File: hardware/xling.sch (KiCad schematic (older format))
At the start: 51 parts, among them J3 MCP73831, J4 USB_OTG, J5 AVR ISP, J6 Battery, Q1 TP0610T, SW2 Up, SW3 Select, SW4 Down, U1 LT1109CZ-12, U2 ATMEGA328P-AU, U3 DEP_128064I, U4 MCP1640B-CH, U5 LM1117-3.3, Y1 8MHz

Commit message: patch 0.1.18: Add new KiCad modules and scheme changes.
Signed-off-by: Dmitry Salychev <darkness.bsd@gmail.com>
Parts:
- removed C12: 2.2uF, Capacitors_SMD:C_0603, symbol C
- removed D1: charging, LEDs:LED_0603, symbol LED
- removed D2: charged, LEDs:LED_0805, symbol LED
- added C9: 1pF, Capacitors_SMD:C_0805, symbol C
- added Q2: NTR0202PL, TO_SOT_Packages_SMD:SOT-23, symbol NTR2101P
- added Q3: NTA4153N, Xling Footprints:SC-75_SOT-416, symbol 2N7000
- added R10: 100K, Resistors_SMD:R_1206, symbol R
- J6: footprint Pin_Headers:Pin_Header_Straight_1x02 -> Xling Footprints:Pin_Header_Straight_1x02
- R1, R5: value 470R -> 100K; Model CRCW1206470RFKTABC -> (none)
- U5: footprint TO_SOT_Packages_SMD:SOT-223-3Lead_TabPin2 -> Xling Footprints:SOT-223-3Lead_TabPin2
- Y1: footprint Crystals:Crystal_HC49-SD_SMD -> Xling Footprints:Crystal_HC49-SD_SMD
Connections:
- net +12V: now also R5.1, Q2.2 (S); no longer U3.23 (VCC)
- net +3V3: now also R1.1; no longer U3.9 (RES#)
- net GND: now also C9.2, Q3.1 (S), R10.2; no longer R5.1
- net BAT_STAT: now reaches J3.1 (STAT)
- net BAT_STAT: now also U2.9 ((PCINT21/OC0B/T1)PD5)
- net at R5.2: now also Q2.1 (G), Q3.3 (D)
- net at C4.1, D5.1 (K), Q1.1 (G)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: no longer R1.1
- net OLED_RES: now reaches R1.2
- net OLED_RES: now also U2.1 ((PCINT19/OC2B/INT1)PD3), U3.9 (RES#)
- net OLED_PWR: now reaches U2.2 ((PCINT20/XCK/T0)PD4)
- net OLED_PWR: now also Q3.2 (G), R10.1
- new net OLED_VCC: C9.1, Q2.3 (D), U3.23 (VCC)
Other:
- note added: "*\n* Including model files\n*\n*.include NTA4001NT1.LIB\n.include NTA4153N.REV0.LIB\n.include NTR0202PL.REV0.LIB\n*\n* Components of the scheme\n*\nR1 0 1 100k\nR2 2 3 100k\n* R3 - pull-down resistor to prove an output is floating contact when\n* XQ2 is closed\n*R3 4 0 100k\nC1 4 0 1p\nXQ1 2 1 0 nta4153n\nXQ2 4 2 3 ntr0202plt1\nVIN 1 0 pulse (0 3.15 2ms 0ns 0ms 5ms 10ms)\nVDD 3 0 pwl (0 0 0ms 0 0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"
- note added: "12V OLED Vcc switch"
- note added: "12V OLED Vcc switch (transient analysis)"
- note added: "3.3V power supply and battery charger"
- note added: "Buttons for microcontroller"
- note added: "Controller:\nVDD:\nVCC:\nMode:\nAddress:"
- note added: "It is recommended to set Iref to 10±2uA:\nR2 = (Vcc-3)/Iref = (12V-3V)/10uA = 900kΩ"
- note added: "Microcontroller ATMEGA328P"
- note added: "OLED display 128x64"
- note added: "SSD1309ZC\n2.8-3.3V\n12V\nI2C\n0x3D"
- note added: "The main idea of the scheme is to produce 3.3V. This can\nbe done by providing a 5V USB connection to power the whole\nscheme via LM1117 and charge a 3.7V Li-Ion or Li-Polymer\nbattery using MCP73831 on the one hand. On the other hand\n- the whole scheme can work autonomously using the battery\nand change its voltage down to 3.3V via MCP1640B."
- note added: "This switch is based on N-Channel and\nP-Channel MOSFETs to power on and off\nOLED display. This is necessary to use\na logic level 3.3V to switch 12V and\nleave Vcc contact floating when\nNTR0202PL is closed."
- note removed: "3.7V Li-Ion, Li-Polymer Battery Charger Curcuit with Load Sharing"
- note removed: "Controller:\nVDD:\nMode:\nAddress:"
- note removed: "It is recommended to set Iref to 10±2uA:\nR = (Vcc-3)/Iref = (12V-3V)/10uA = 900kΩ"
- note removed: "SSD1309ZC\n2.8-3.3V\nI2C\n0x3D"
- note removed: "both are tantalum capacitors\nAVX TAJB106K006RNJ\n"
- moved on the sheet: C1, C10, C11, C13, C15, C18, C19, C2, C20, C3, C4, C5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

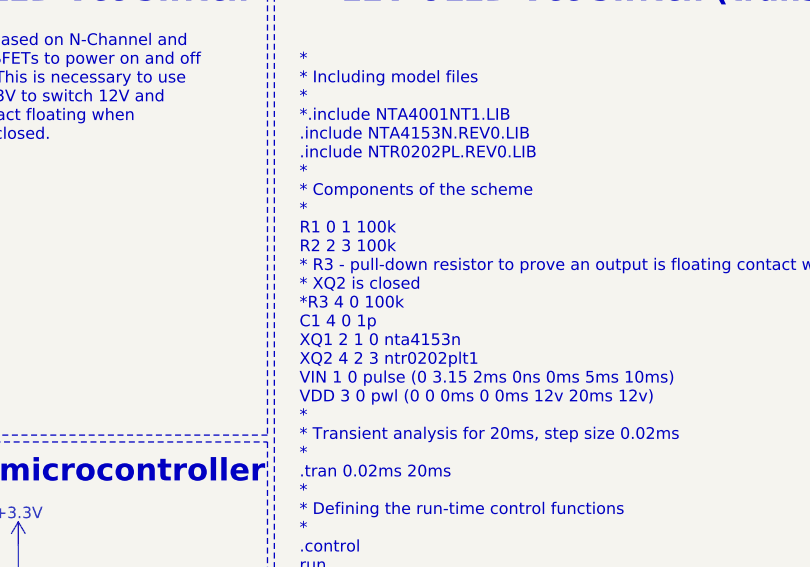
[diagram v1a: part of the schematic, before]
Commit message: patch 0.1.20: Update PCB and prepare gerber files for production.
Signed-off-by: Dmitry Salychev <darkness.bsd@gmail.com>
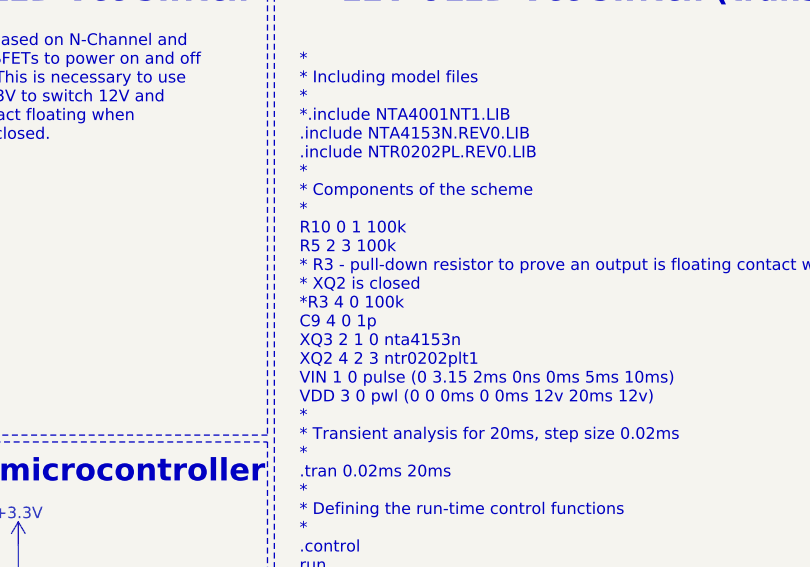
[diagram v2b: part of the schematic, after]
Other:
- note added: "*\n* Including model files\n*\n*.include NTA4001NT1.LIB\n.include NTA4153N.REV0.LIB\n.include NTR0202PL.REV0.LIB\n*\n* Components of the scheme\n*\nR10 0 1 100k\nR5 2 3 100k\n* R3 - pull-down resistor to prove an output is floating contact when\n* XQ2 is closed\n*R3 4 0 100k\nC9 4 0 1p\nXQ3 2 1 0 nta4153n\nXQ2 4 2 3 ntr0202plt1\nVIN 1 0 pulse (0 3.15 2ms 0ns 0ms 5ms 10ms)\nVDD 3 0 pwl (0 0 0ms 0 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"
- note removed: "*\n* Including model files\n*\n*.include NTA4001NT1.LIB\n.include NTA4153N.REV0.LIB\n.include NTR0202PL.REV0.LIB\n*\n* Components of the scheme\n*\nR1 0 1 100k\nR2 2 3 100k\n* R3 - pull-down resistor to prove an output is floating contact when\n* XQ2 is closed\n*R3 4 0 100k\nC1 4 0 1p\nXQ1 2 1 0 nta4153n\nXQ2 4 2 3 ntr0202plt1\nVIN 1 0 pulse (0 3.15 2ms 0ns 0ms 5ms 10ms)\nVDD 3 0 pwl (0 0 0ms 0 0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"
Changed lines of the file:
@@
 Title "Xling Schematic"
 Date ""
-Rev "0.1.18"
-Comp "Terrible Terminal Inc."
+Rev "0.1.20"
+Comp ""
 Comment1 ""
 Comment2 ""
@@
 This switch is based on N-Channel and\nP-Channel MOSFETs to power on and off\nOLED display. This is necessary to use\na logic level 3.3V to switch 12V and\nleave Vcc contact floating when\nNTR0202PL is closed.
 Text Notes 12340 3970 0    51   ~ 0
-*\n* Including model files\n*\n*.include NTA4001NT1.LIB\n.include NTA4153N.REV0.LIB\n.include NTR0202PL.REV0.LIB\n*\n* Components of the scheme\n*\nR1 0 1 100k\nR2 2 3 100k\n* R3 - pull-down resistor to prove an output is floating contact when\n* XQ2 is closed\n*R3 4 0 100k\nC1 4 0 1p\nXQ1 2 1 0 nta4153n\nXQ2 4 2 3 ntr0202plt1\nVIN 1 0 pulse (0 3.15 2ms 0ns 0ms 5ms 10ms)\nVDD 3 0 pwl (0 0 0ms 0 0ms 12v 20ms 12v)\n*\n* Transient analysis for 20ms, step size 0.02ms\n*\n.tran 0.02ms 20ms\n*\n* Defining the run-time control functions\n*\n.control\nrun\n*\n* Plotting input and output voltages\n*\nplot v(1) v(4)\n.endc\n.end
+*\n* Including model files\n*\n*.include NTA4001NT1.LIB\n.include NTA4153N.REV0.LIB\n.include NTR0202PL.REV0.LIB\n*\n* Components of the scheme\n*\nR10 0 1 100k\nR5 2 3 100k\n* R3 - pull-down resistor to prove an output is floating contact when\n* XQ2 is closed\n*R3 4 0 100k\nC9 4 0 1p\nXQ3 2 1 0 nta4153n\nXQ2 4 2 3 ntr0202plt1\nVIN 1 0 pulse (0 3.15 2ms 0ns 0ms 5ms 10ms)\nVDD 3 0 pwl (0 0 0ms 0 0ms 12v 20ms 12v)\n*\n* Transient analysis for 20ms, step size 0.02ms\n*\n.tran 0.02ms 20ms\n*\n* Defining the run-time control functions\n*\n.control\nrun\n*\n* Plotting input and output voltages\n*\nplot v(1) v(4)\n.endc\n.end
 Wire Notes Line
 	12230 780  12230 4080

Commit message: patch 0.1.21: Correct exact models of the components in schematic.
Signed-off-by: Dmitry Salychev <darkness.bsd@gmail.com>
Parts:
- C13, C15: Model C0805C220J5GACTU -> CL21C220JBANNNC
- C18, C19, C20, C7: Model C0805C472K5RACTU -> CC0805KRX7R9BB472
- C8: Model 08055C104K4T2A -> CL21B104JBCNNNC
- C9: Model (none) -> CL21C010BBANNNC
- R1, R10, R5: Model (none) -> CRCW1206100KFKTABC
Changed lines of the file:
@@
 Title "Xling Schematic"
 Date ""
-Rev "0.1.20"
+Rev "0.1.21"
 Comp ""
 Comment1 ""
@@
 F 2 "Capacitors_SMD:C_0805" H 4388 2720 50  0001 C CNN
 F 3 "" H 4350 2870 50  0001 C CNN
-F 4 "C0805C220J5GACTU" V 4350 2870 60  0001 C CNN "Model"
+F 4 "CL21C220JBANNNC" V 4350 2870 60  0001 C CNN "Model"
 	1    4350 2870
 	0    -1   1    0
@@
 F 2 "Capacitors_SMD:C_0805" H 4388 3020 50  0001 C CNN
 F 3 "" H 4350 3170 50  0001 C CNN
-F 4 "C0805C220J5GACTU" V 4350 3170 60  0001 C CNN "Model"
+F 4 "CL21C220JBANNNC" V 4350 3170 60  0001 C CNN "Model"
 	1    4350 3170
 	0    -1   1    0
@@
 F 2 "Capacitors_SMD:C_0805" H 1848 1460 50  0001 C CNN
 F 3 "" H 1810 1610 50  0001 C CNN
-F 4 "08055C104K4T2A" H 1810 1610 60  0001 C CNN "Model"
+F 4 "CL21B104JBCNNNC" H 1810 1610 60  0001 C CNN "Model"
 	1    1810 1610
 	1    0    0    -1
@@
 F 2 "Capacitors_SMD:C_0805" H 1538 1460 50  0001 C CNN
 F 3 "" H 1500 1610 50  0001 C CNN
-F 4 "C0805C472K5RACTU" H 1500 1610 60  0001 C CNN "Model"
+F 4 "CC0805KRX7R9BB472" H 1500 1610 60  0001 C CNN "Model"
 	1    1500 1610
 	1    0    0    -1
@@
 F 2 "Capacitors_SMD:C_0805" H 9328 4150 50  0001 C CNN
 F 3 "" H 9290 4300 50  0001 C CNN
-F 4 "C0805C472K5RACTU" H 9290 4300 60  0001 C CNN "Model"
+F 4 "CC0805KRX7R9BB472" H 9290 4300 60  0001 C CNN "Model"
 	1    9290 4300
 	1    0    0    -1
@@
 F 2 "Capacitors_SMD:C_0805" H 10598 4140 50  0001 C CNN
 F 3 "" H 10560 4290 50  0001 C CNN
-F 4 "C0805C472K5RACTU" H 10560 4290 60  0001 C CNN "Model"
+F 4 "CC0805KRX7R9BB472" H 10560 4290 60  0001 C CNN "Model"
 	1    10560 4290
 	1    0    0    -1
@@
 F 2 "Capacitors_SMD:C_0805" H 11808 4130 50  0001 C CNN
 F 3 "" H 11770 4280 50  0001 C CNN
-F 4 "C0805C472K5RACTU" H 11770 4280 60  0001 C CNN "Model"
+F 4 "CC0805KRX7R9BB472" H 11770 4280 60  0001 C CNN "Model"
 	1    11770 4280
 	1    0    0    -1
@@
 F 2 "Resistors_SMD:R_1206" V 5980 1970 50  0001 C CNN
 F 3 "" H 6050 1970 50  0001 C CNN
+F 4 "CRCW1206100KFKTABC" V 6050 1970 60  0001 C CNN "Model"
 	1    6050 1970
 	1    0    0    -1
@@
 F 2 "Resistors_SMD:R_1206" V 8960 2330 50  0001 C CNN
 F 3 "" H 9030 2330 50  0001 C CNN
+F 4 "CRCW1206100KFKTABC" V 9030 2330 60  0001 C CNN "Model"
 	1    9030 2330
 	1    0    0    -1
@@
 F 2 "Resistors_SMD:R_1206" V 9450 1570 50  0001 C CNN
 F 3 "" H 9520 1570 50  0001 C CNN
+F 4 "CRCW1206100KFKTABC" V 9520 1570 60  0001 C CNN "Model"
 	1    9520 1570
 	1    0    0    -1
@@
 F 2 "Capacitors_SMD:C_0805" H 10158 2160 50  0001 C CNN
 F 3 "" H 10120 2310 50  0001 C CNN
+F 4 "CL21C010BBANNNC" H 10120 2310 60  0001 C CNN "Model"
 	1    10120 2310
 	1    0    0    -1

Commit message: patch 0.1.22: Power supply scheme modified and PCB update.
Signed-off-by: Dmitry Salychev <darkness.bsd@gmail.com>
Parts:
- removed C2, C4: 10uF, Capacitors_Tantalum_SMD:CP_Tantalum_Case-B_EIA-3528-21_Reflow, symbol CP
- removed Q1: TP0610T, TO_SOT_Packages_SMD:SOT-23, symbol TP0610T
- removed Q3: NTA4153N, Xling Footprints:SC-75_SOT-416, symbol 2N7000
- removed U5: LM1117-3.3, Xling Footprints:SOT-223-3Lead_TabPin2, symbol LM1117-3.3
- added Q1: NTR0202PL, TO_SOT_Packages_SMD:SOT-23, symbol NTR2101P
- added Q3: NTA4153N, Xling Footprints:SC-75_SOT-416, symbol NTA4153N
- added R11: 191K, Resistors_SMD:R_0805, symbol R
- added R12: 110K, Resistors_SMD:R_0805, symbol R
- R3: value 2K2 -> 2K7; Model CRCW12062K20FKTABC -> 1206S4J0272T5E
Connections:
- net +12V: now also U3.23 (VCC); no longer Q2.2 (S), R5.1
- net +3V3: now also Q2.2 (S), R5.1; no longer L2.1
- net GND: now also Q3.2 (S), R12.2
- net OLED_PWR: now also Q3.1 (G)
- net OLED_VCC: now also L2.1; no longer U3.23 (VCC)
- net at C6.1, J3.3 (VBAT), J6.1 (Pin_1): now also Q1.3 (D), R11.1
- net at C3.1, D5.2 (A), J3.4 (VDD)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: now also R4.1, Q1.1 (G)
- net at D5.1 (K): now also C5.1, L1.1, U4.3 (EN), U4.6 (VIN), Q1.2 (S); no longer R4.1
- net BAT_LVL: now reaches U2.23 ((PCINT8/ADC0)PC0)
- net BAT_LVL: now also R11.2, R12.1
- net at Q2.1 (G), R5.2: now also Q3.3 (D)
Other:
- note added: "Charge current regulation:\nIreg = 1000V/Rprog, where\nIreg - charge current, in mA\nRprog - resistor value (R3), in kOhm.\n\nRprog = 1000/380 ~~ 2.6316kOhm,\nStandard value is 2.7kOhm, Ireg ~~ 370mA"
- note added: "Current Direction Control Circuit based on a single P-Channel MOSFET\n\n* Including model files\n*.include NTA4001NT1.LIB\n.include NTA4153N.REV0.LIB\n.include NTR0202PL.REV0.LIB\n.include 1N5819.LIB\n\n* Components of the scheme\nR1 0 1 100k\nR2 0 2 12\nC1 0 3 4.7u\nC2 0 2 4.7u\nXQ1 3 1 2 ntr0202plt1\nD1 1 2 D1n5819\nVIN 1 0 pulse (0 4.95 2ms 0ns 0ms 5ms 10ms)\nVDD 3 0 pwl (0 0 0ms 0 0ms 3.2v 20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"
- note added: "Current Direction Control Circuit\nbased on a single P-channel MOSFET\n(part of a battery charger)"
- note added: "SSD1309ZC\n2.8-3.3V\n12V\nI2C\n0x7A"
- note added: "The main idea of a scheme is to produce 3.3V and charge a battery\nif it needs using load-sharing. This can be done by providing a 5V USB \nconnection to power the whole circuit via LM1117 and\ncharge a 3.7V Li-Ion or Li-Polymer battery using MCP73831 on one hand.\nOn the other hand, it can work autonomously using the battery and\nchanging its voltage down to 3.3V via MCP1640B."
- note added: "max.\n45mA"
- note removed: "45mA max"
- note removed: "SSD1309ZC\n2.8-3.3V\n12V\nI2C\n0x3D"
- note removed: "The main idea of the scheme is to produce 3.3V. This can\nbe done by providing a 5V USB connection to power the whole\nscheme via LM1117 and charge a 3.7V Li-Ion or Li-Polymer\nbattery using MCP73831 on the one hand. On the other hand\n- the whole scheme can work autonomously using the battery\nand change its voltage down to 3.3V via MCP1640B."
- moved on the sheet: C1, C10, C13, C15, C3, C5, C6, D3, D5, J3, J4, J6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

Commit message: patch 0.2.0: Update hardware files to KiCad 5.
This patch brought a firmware part of the project to perform any tests
only. It draws two different pictures on an OLED display and counts
frames per second.

Schematic was updated to include a new DC-DC buck converter (AP3401) to
produce 3.3V from both USB and a battery. Choosing this converter is a
trade-off between an expensive buck-boost converter which can operate
correctly at 3.2V voltage level of almost depleted battery and a cheap buck
converter which produces 3.3V from the input voltage which should be above
the required level.

There is also a python plugin in hardware/plugins directory to generate a BOM
html file. It can be added to and called from KiCad directly.

Signed-off-by: Dmitry Salychev <darkness.bsd@gmail.com>
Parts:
- removed C1: 10uF, Capacitors_SMD:C_0805, symbol C
- removed J3: MCP73831, Xling Footprints:MCP73831_SOT_23, symbol MCP73831
- removed L1: 4.7uH, Inductors_SMD:L_1210, symbol L
- removed R6: 191K, Resistors_SMD:R_0805, symbol R
- removed R7: 110K, Resistors_SMD:R_0805, symbol R
- removed U4: MCP1640B-CH, TO_SOT_Packages_SMD:SOT-23-6, symbol MCP1640B-CH
- added C1: 22pF, Xling Footprints:C_0805_2012Metric, symbol xling:C
- added C2: 4.7uF, Xling Footprints:C_1206_3216Metric, symbol xling:C
- added L1: 2.2uH, Xling Footprints:L_1210_3225Metric, symbol xling:L
- added R13, R6: 100K, Xling Footprints:R_1206_3216Metric, symbol xling:R
- added R20: 110K, Xling Footprints:R_0805_2012Metric, symbol xling:R
- added R7: 510K, Xling Footprints:R_0603_1608Metric, symbol xling:R
- added U4: MCP73831, Xling Footprints:MCP73831_SOT_23, symbol xling:MCP73831
- added U5: AP3401_TSOT26, symbol xling:AP3401_TSOT26
- C10: footprint Capacitors_Tantalum_SMD:CP_Tantalum_Case-C_EIA-6032-28_Reflow -> Xling Footprints:CP_EIA-6032-20_AVX-F; symbol CP -> xling:CP
- C11: footprint Capacitors_SMD:C_0603 -> Xling Footprints:C_0603_1608Metric; symbol C -> xling:C
- C13, C15, C18, C19, C20, C7, C8, C9: footprint Capacitors_SMD:C_0805 -> Xling Footprints:C_0805_2012Metric; symbol C -> xling:C
- C3, C5, C6: footprint Capacitors_SMD:C_1206 -> Xling Footprints:C_1206_3216Metric; symbol C -> xling:C
- D3: footprint Diodes_THT:D_DO-41_SOD81_P7.62mm_Horizontal -> Xling Footprints:D_DO-41_SOD81_P7.62mm_Horizontal; symbol 1N5818 -> xling:1N5818
- D5: footprint Diodes_THT:D_DO-41_SOD81_P7.62mm_Horizontal -> Xling Footprints:D_DO-41_SOD81_P7.62mm_Horizontal; symbol B320 -> xling:1N5818
- J4: footprint Connectors:USB_Mini-B -> Xling Footprints:USB_Mini-B_Lumberg_2486_01_Horizontal; symbol USB_OTG -> xling:USB_OTG; Model 675031020 -> Molex 67503-1020
- J5: footprint Socket_Strips:Socket_Strip_Straight_2x03_Pitch2.54mm -> Xling Footprints:IDC-Header_2x03_P2.54mm_Vertical; symbol Conn_02x03_Odd_Even -> xling:Conn_02x03_Odd_Even; Model empty -> T821106A1S100CEU
- J6: symbol Conn_01x02 -> xling:Conn_01x02; Model empty -> None
- L2: footprint Inductors_SMD:L_7.3x7.3_H3.5 -> Xling Footprints:L_7.3x7.3_H3.5; symbol L_Core_Ferrite -> xling:L_Core_Ferrite
- Q1, Q2: footprint TO_SOT_Packages_SMD:SOT-23 -> Xling Footprints:SOT-23; symbol NTR2101P -> xling:NTR2101P
- Q3: symbol NTA4153N -> xling:NTA4153N
- R1, R10, R17, R18, R19, R2, R4, R5: footprint Resistors_SMD:R_1206 -> Xling Footprints:R_1206_3216Metric; symbol R -> xling:R
- R11, R12: footprint Resistors_SMD:R_0805 -> Xling Footprints:R_0805_2012Metric; symbol R -> xling:R
- R14, R15, R16, R8, R9: footprint Resistors_SMD:R_0603 -> Xling Footprints:R_0603_1608Metric; symbol R -> xling:R
- R3: value 2K7 -> 4K3; footprint Resistors_SMD:R_1206 -> Xling Footprints:R_0603_1608Metric; symbol R -> xling:R; Model 1206S4J0272T5E -> 0603SAJ0432T5E
- SW2: value Up -> BTN; footprint Buttons_Switches_SMD:SW_SPST_PTS645 -> Xling Footprints:SW_SPST_PTS645; symbol SW_Push -> xling:SW_Push; Note (none) -> UP button
- SW3: value Select -> BTN; footprint Buttons_Switches_SMD:SW_SPST_PTS645 -> Xling Footprints:SW_SPST_PTS645; symbol SW_Push -> xling:SW_Push; Note (none) -> SELECT Button
- SW4: value Down -> BTN; footprint Buttons_Switches_SMD:SW_SPST_PTS645 -> Xling Footprints:SW_SPST_PTS645; symbol SW_Push -> xling:SW_Push; Note (none) -> DOWN Button
- U1: symbol LT1109CZ-12 -> xling:LT1109CZ-12
- U2: footprint Housings_QFP:TQFP-32_7x7mm_Pitch0.8mm -> Xling Footprints:TQFP-32_7x7mm_P0.8mm; symbol ATMEGA328P-AU -> xling:ATMEGA328P-AU
- U3: symbol DEP_128064I -> xling:DEP_128064I; Model XF2M24151AR100,DEP128064I-Y -> XF2M24151AR100, DEP128064I-Y
- Y1: symbol Crystal -> xling:Crystal
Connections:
- net +3V3: now also C1.1, C2.1, L1.2, R7.2
- net BAT_STAT: now also U4.1 (STAT)
- net GND: now also C2.2, R20.1, U4.2 (VSS), U5.2 (GND)
- net at C6.1, J6.1 (Pin_1), Q1.3 (D)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: now also U4.3 (VBAT)
- net at C3.1, D5.2 (A), J4.1 (VBUS)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: now also U4.4 (VDD)
- net at R3.1: now also U4.5 (PROG)
- net at C5.1, D5.1 (K), Q1.2 (S): now also R13.2, R6.2, U5.4 (VIN)
- new net: R6.1, U5.1 (EN)
- new net: L1.1, U5.3 (LX)
- new net: R13.1, U5.5 (PG)
- new net: C1.2, R20.2, R7.1, U5.6 (FB)
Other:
- note added: "3.3V-to-12V DC-DC"
- note added: "3.3V-to-12V Switch"
- note added: "3.3V-to-12V Switch (ngspice .cir)"
- note added: "Battery (charge) current regulator\nbased on a resistor R3:\n\nIreg = 1000V/Rprog, where\nIreg - charge current, in mA\nRprog - resistor value (R3), in kOhm.\n\nRprog = 1000/250 = 4kOhm,\nStandard value is 4.3kOhm, Ireg ~~ 232mA"
- note added: "Control Buttons"
- note added: "Current Direction (Q1 based, ngspice .cir)"
- note added: "Main microcontroller"
- note added: "OLED display"
- note added: "Power supply and battery charger"
- note added: "Resistor devider:\nR6 = R7*(Vout/0.6-1) =\n(110*10^3)*(3.3/0.6-1) ~~ 510kOhm"
- note added: "The main idea of a scheme is to produce 3.3V and charge\na battery sharing load between a USB power and a power\nobtained from the battery."
- note added: "This can be achieved by providing a 5V USB (~~4.6V after\nvoltage drop on D5) to fill needs of the whole circuit via\nAP3401 and charge a 3.7V Li-Ion or Li-Polymer battery\nusing MCP73831 battery controller, on one hand (Q1 will be\nclosed in this case). On the other, the whole scheme can work \nautonomously using the battery and changing its voltage\ndown to 3.3V via AP3401 (Q1 will be open)."
- note removed: "12V OLED Vcc switch"
- note removed: "12V OLED Vcc switch (transient analysis)"
- note removed: "3.3V power supply and battery charger"
- note removed: "3.3V to 12V, 45mA DC-DC for OLED panel"
- note removed: "Buttons for microcontroller"
- note removed: "Charge current regulation:\nIreg = 1000V/Rprog, where\nIreg - charge current, in mA\nRprog - resistor value (R3), in kOhm.\n\nRprog = 1000/380 ~~ 2.6316kOhm,\nStandard value is 2.7kOhm, Ireg ~~ 370mA"
- note removed: "Current Direction Control Circuit\nbased on a single P-channel MOSFET\n(part of a battery charger)"
- note removed: "Microcontroller ATMEGA328P"
- note removed: "OLED display 128x64"
- note removed: "Resistor devider:\nR6 = R7*(Vout/1.21-1) =\n(110*10^3)*(3.3/1.21-1) = 190kOhm"
- note removed: "The main idea of a scheme is to produce 3.3V and charge a battery\nif it needs using load-sharing. This can be done by providing a 5V USB \nconnection to power the whole circuit via LM1117 and\ncharge a 3.7V Li-Ion or Li-Polymer battery using MCP73831 on one hand.\nOn the other hand, it can work autonomously using the battery and\nchanging its voltage down to 3.3V via MCP1640B."
- moved on the sheet: C3, C5, C6, D5, J4, J5, J6, Q1, R11, R12, R3, R4
